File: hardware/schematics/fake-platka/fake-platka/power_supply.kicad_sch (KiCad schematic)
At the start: 6 parts, among them J1 XT60PW-F, J2 XT60PW-F, U1 XL4005, U5 XL4005

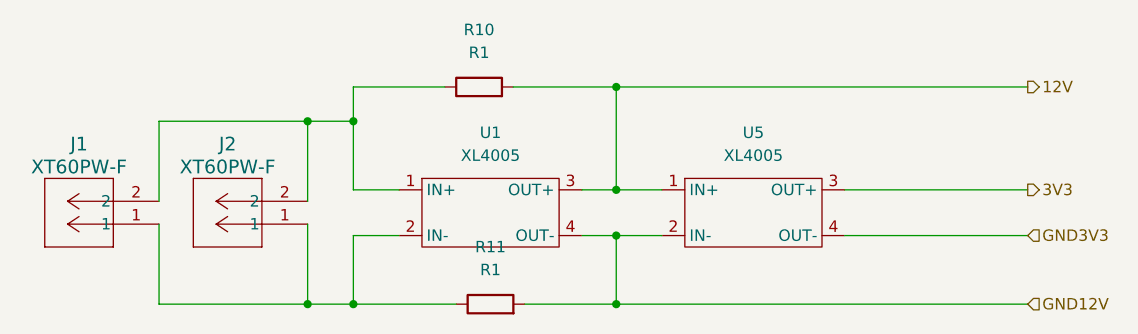
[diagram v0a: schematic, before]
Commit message: added all components to the schematic and pcb
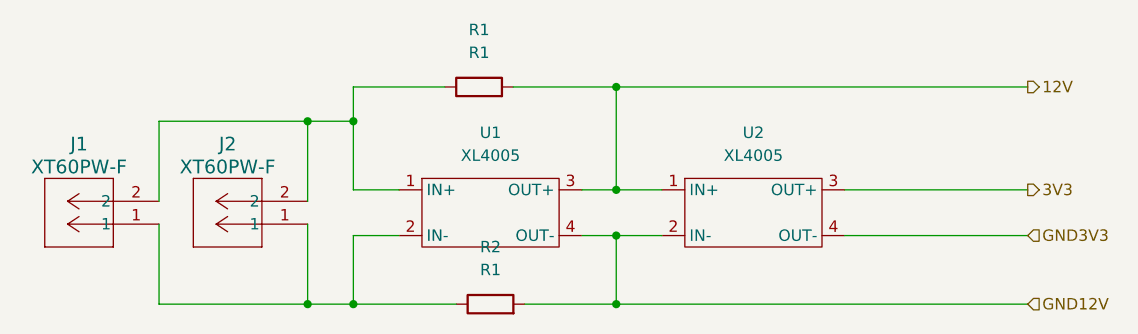
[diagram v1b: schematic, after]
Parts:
- removed U5: XL4005, quadruped-lib-footprints:XL4005_DC-DC, symbol library:XL4005
- added U2: XL4005, quadruped-lib-footprints:XL4005_DC-DC, symbol library:XL4005
- renumbered R10 to R1, R11 to R2
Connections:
- net 12V: now also U2.1 (IN+)
- net 3V3: now also U2.3 (OUT+)
- net GND12V: now also U2.2 (IN-)
- net GND3V3: now also U2.4 (OUT-)
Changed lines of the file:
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@@
     (pin "2")
+  )
+  (symbol (lib_id "library:XL4005") (at 130.81 62.23 0) (unit 1)
+    (in_bom yes) (on_board yes) (fields_autoplaced)
+    (property "Reference" "U2" (id 0) (at 130.81 59.69 0))
+    (property "Value" "XL4005" (id 1) (at 130.81 62.23 0))
+    (property "Footprint" "quadruped-lib-footprints:XL4005_DC-DC" (id 2) (at 130.81 62.23 0)
+      (effects (font (size 1.27 1.27)) hide)
+    )
+    (property "Datasheet" "" (id 3) (at 130.81 62.23 0)
+      (effects (font (size 1.27 1.27)) hide)
+    )
+    (pin "1")
+    (pin "2")
+    (pin "3")
+    (pin "4")
+  )
+  (symbol (lib_name "XL4005_1") (lib_id "library:XL4005") (at 101.6 62.23 0) (unit 1)
+    (in_bom yes) (on_board yes) (fields_autoplaced)
+    (property "Reference" "U1" (id 0) (at 101.6 59.69 0))
+    (property "Value" "XL4005" (id 1) (at 101.6 62.23 0))
+    (property "Footprint" "quadruped-lib-footprints:XL4005_DC-DC" (id 2) (at 101.6 62.23 0)
+      (effects (font (size 1.27 1.27)) hide)
+    )
+    (property "Datasheet" "" (id 3) (at 101.6 62.23 0)
+      (effects (font (size 1.27 1.27)) hide)
+    )
+    (pin "1")
+    (pin "2")
+    (pin "3")
+    (pin "4")
   )
   (symbol (lib_id "library:XT60PW-F") (at 64.77 69.85 180) (unit 1)
@@
   (symbol (lib_id "Device:R") (at 100.33 54.61 90) (unit 1)
     (in_bom yes) (on_board yes) (fields_autoplaced)
-    (property "Reference" "R10" (id 0) (at 100.33 48.26 90))
+    (property "Reference" "R1" (id 0) (at 100.33 48.26 90))
     (property "Value" "R1" (id 1) (at 100.33 50.8 90))
     (property "Footprint" "Resistor_THT:R_Axial_DIN0207_L6.3mm_D2.5mm_P10.16mm_Horizontal" (id 2) (at 100.33 56.388 90)
@@
   (symbol (lib_id "Device:R") (at 101.6 78.74 90) (unit 1)
     (in_bom yes) (on_board yes) (fields_autoplaced)
-    (property "Reference" "R11" (id 0) (at 101.6 72.39 90))
+    (property "Reference" "R2" (id 0) (at 101.6 72.39 90))
     (property "Value" "R1" (id 1) (at 101.6 74.93 90))
     (property "Footprint" "Resistor_THT:R_Axial_DIN0207_L6.3mm_D2.5mm_P10.16mm_Horizontal" (id 2) (at 101.6 80.518 90)
@@
     (pin "2")
   )
-  (symbol (lib_id "library:XL4005") (at 101.6 62.23 0) (unit 1)
-    (in_bom yes) (on_board yes) (fields_autoplaced)
-    (property "Reference" "U1" (id 0) (at 101.6 59.69 0))
-    (property "Value" "XL4005" (id 1) (at 101.6 62.23 0))
-    (property "Footprint" "quadruped-lib-footprints:XL4005_DC-DC" (id 2) (at 101.6 62.23 0)
-      (effects (font (size 1.27 1.27)) hide)
-    )
-    (property "Datasheet" "" (id 3) (at 101.6 62.23 0)
-      (effects (font (size 1.27 1.27)) hide)
-    )
-    (pin "1")
-    (pin "2")
-    (pin "3")
-    (pin "4")
-  )
-  (symbol (lib_id "library:XL4005") (at 130.81 62.23 0) (unit 1)
-    (in_bom yes) (on_board yes) (fields_autoplaced)
-    (property "Reference" "U5" (id 0) (at 130.81 59.69 0))
-    (property "Value" "XL4005" (id 1) (at 130.81 62.23 0))
-    (property "Footprint" "quadruped-lib-footprints:XL4005_DC-DC" (id 2) (at 130.81 62.23 0)
-      (effects (font (size 1.27 1.27)) hide)
-    )
-    (property "Datasheet" "" (id 3) (at 130.81 62.23 0)
-      (effects (font (size 1.27 1.27)) hide)
-    )
-    (pin "1")
-    (pin "2")
-    (pin "3")
-    (pin "4")
-  )
 )

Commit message: working on pcb and documentation
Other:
- company: (none) -> By Andrey Shefa
- title: (none) -> First pcb for quadruped robot v3
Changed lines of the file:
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@@
 (kicad_sch (version 20211123) (generator eeschema)
   (paper "A4")
+  (title_block
+    (title "First pcb for quadruped robot v3")
+    (date "2024-02-06")
+    (rev "0")
+    (company "By Andrey Shefa")
+  )
   (junction (at 115.57 66.04) (diameter 0) (color 0 0 0 0)
   )
@@
   )
   (symbol (lib_id "Device:R") (at 100.33 54.61 90) (unit 1)
-    (in_bom yes) (on_board yes) (fields_autoplaced)
-    (property "Reference" "R1" (id 0) (at 100.33 48.26 90))
-    (property "Value" "R1" (id 1) (at 100.33 50.8 90))
+    (in_bom yes) (on_board yes)
+    (property "Reference" "R1" (id 0) (at 100.33 49.53 90))
+    (property "Value" "R1" (id 1) (at 100.33 52.07 90))
     (property "Footprint" "Resistor_THT:R_Axial_DIN0207_L6.3mm_D2.5mm_P10.16mm_Horizontal" (id 2) (at 100.33 56.388 90)
       (effects (font (size 1.27 1.27)) hide)
@@
   )
   (symbol (lib_id "Device:R") (at 101.6 78.74 90) (unit 1)
-    (in_bom yes) (on_board yes) (fields_autoplaced)
-    (property "Reference" "R2" (id 0) (at 101.6 72.39 90))
-    (property "Value" "R1" (id 1) (at 101.6 74.93 90))
+    (in_bom yes) (on_board yes)
+    (property "Reference" "R2" (id 0) (at 101.6 73.66 90))
+    (property "Value" "R1" (id 1) (at 101.6 76.2 90))
     (property "Footprint" "Resistor_THT:R_Axial_DIN0207_L6.3mm_D2.5mm_P10.16mm_Horizontal" (id 2) (at 101.6 80.518 90)
       (effects (font (size 1.27 1.27)) hide)
